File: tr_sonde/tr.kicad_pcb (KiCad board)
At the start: 4 copper layers, 104.4 x 65.3 mm, 87 parts, among them J1 SMA, J2 SMA, J3 SMA, K1 TR, K2 HV_MON, K3 VINHDR, Q1 PBSS4250X, Q2 MMBT2222A, Q3 STD2NK90ZT4, Q4 STD2NK90ZT4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

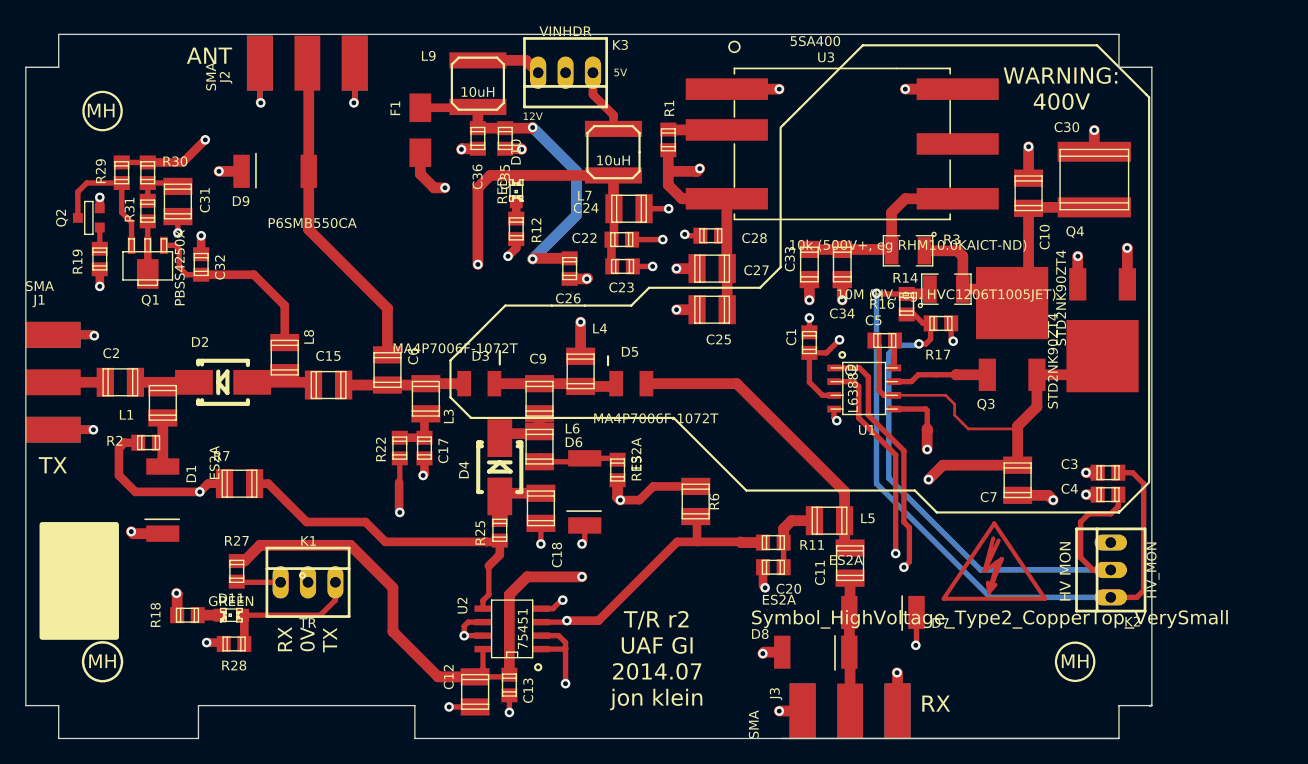
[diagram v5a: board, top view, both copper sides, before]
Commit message: added extra power header to control board, added spam to driver amp bottom soldermask layer to pass oshpark check script, added board outlines to agc and tr silkscreen
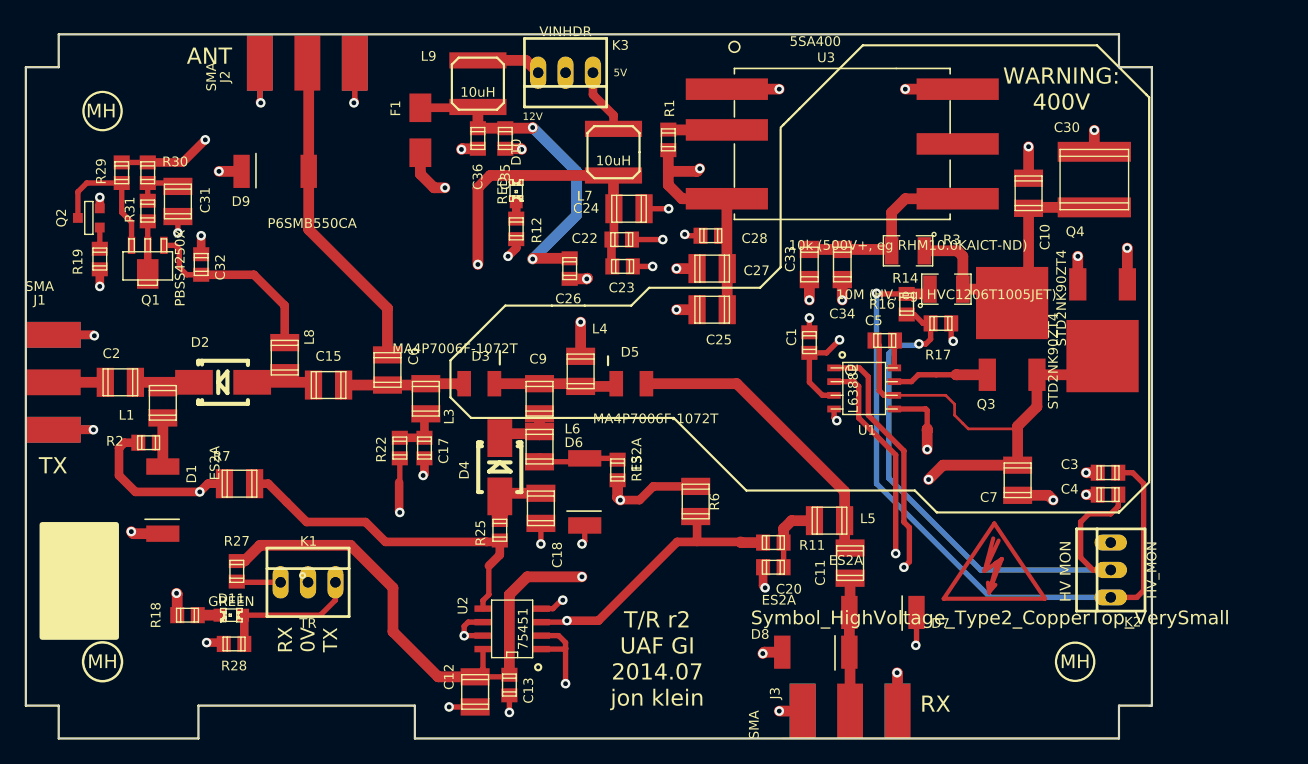
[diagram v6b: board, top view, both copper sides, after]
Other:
- rule trace_min: 0.18 -> 0.2

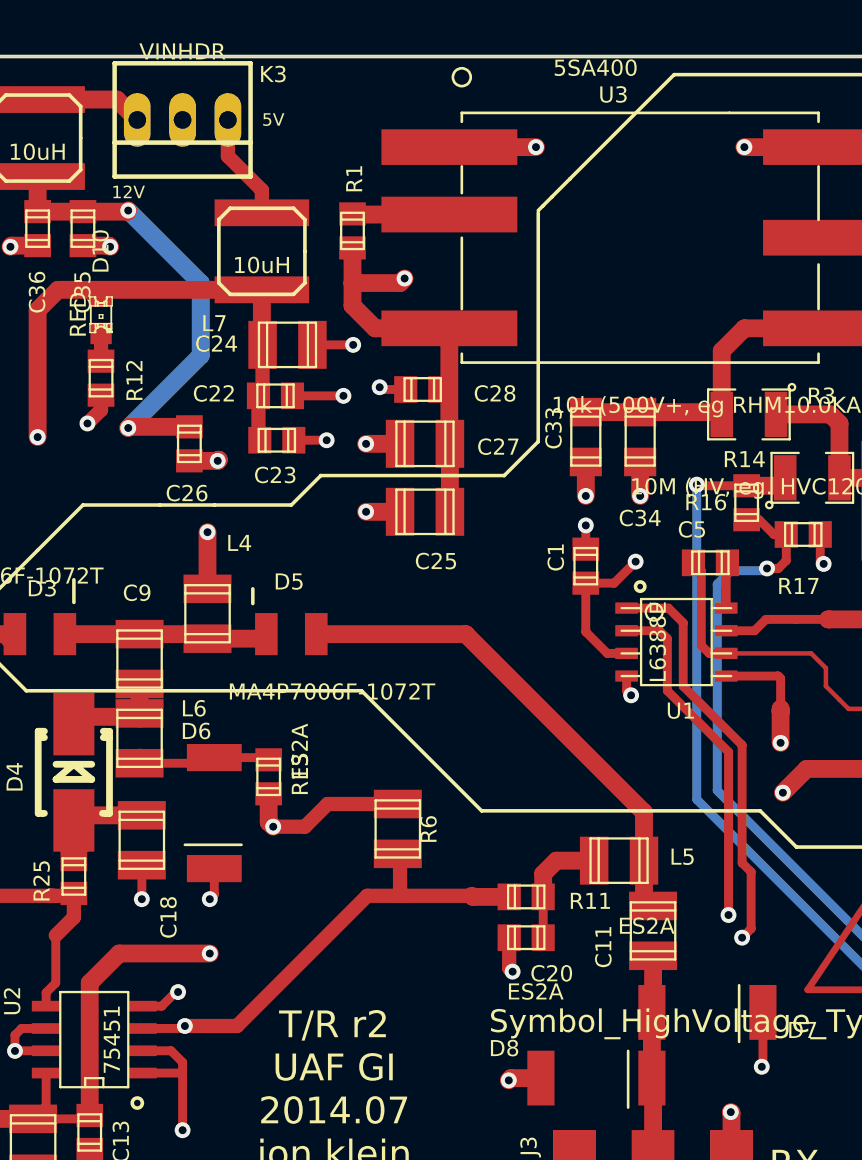
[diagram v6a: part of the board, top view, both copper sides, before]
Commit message: fixed footprints and silkscreen on t/r r2
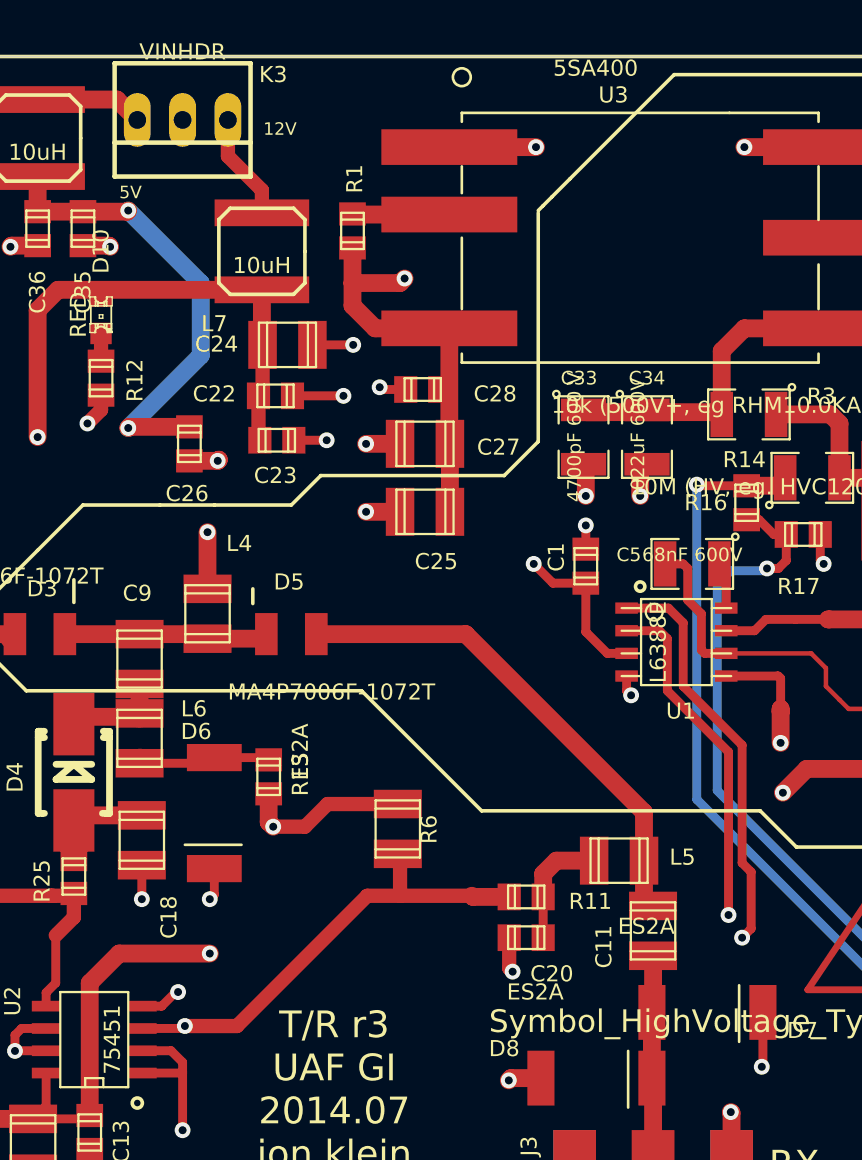
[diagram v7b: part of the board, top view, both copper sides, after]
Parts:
- C33: footprint Capacitors_SMD:c_1206 -> SMD_Packages:SMD-1210
- C34: footprint smd_capacitors:c_1206 -> SMD_Packages:SMD-1210
- C5: footprint smd_capacitors:c_0805 -> SMD_Packages:SMD-1210
- moved C5 1.02 mm to (135.8, 53.3), turned to 180 degrees
- moved C34 0.38 mm to (133.2, 46.2), turned to 270 degrees
- moved C33 0.13 mm to (129.7, 46.2), turned to 270 degrees
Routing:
- net VCC: track 205.8 -> 200.2 mm
- net /hvbias: track 92.7 -> 94.5 mm
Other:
- board text added: "T/R r3 UAF GI 2014.07 jon klein"
- board text added: "high power T/R switch r3"
- board text removed: "T/R r2 UAF GI 2014.07 jon klein"
- board text removed: "high power T/R switch r2"

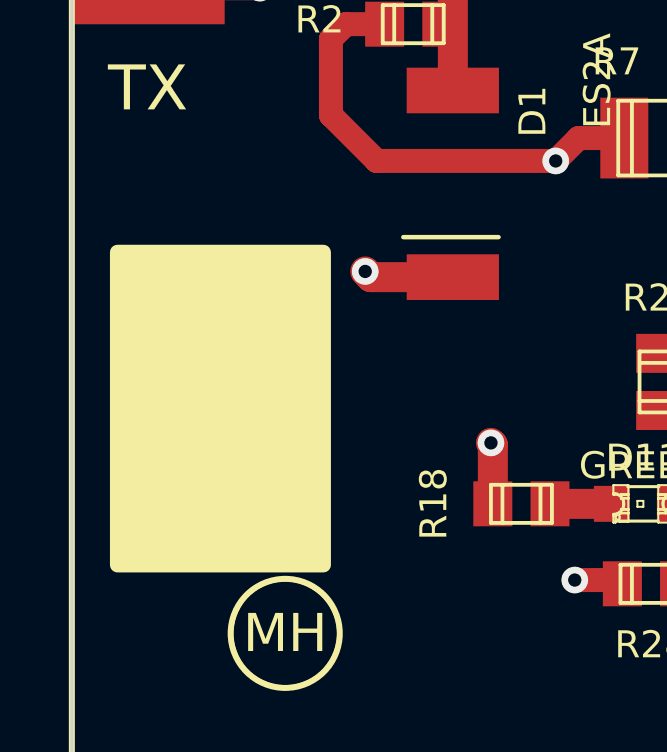
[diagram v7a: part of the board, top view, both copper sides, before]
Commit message: added power distribution board, changed SMA connectors to top through hole, moved mounting holes on rxfe
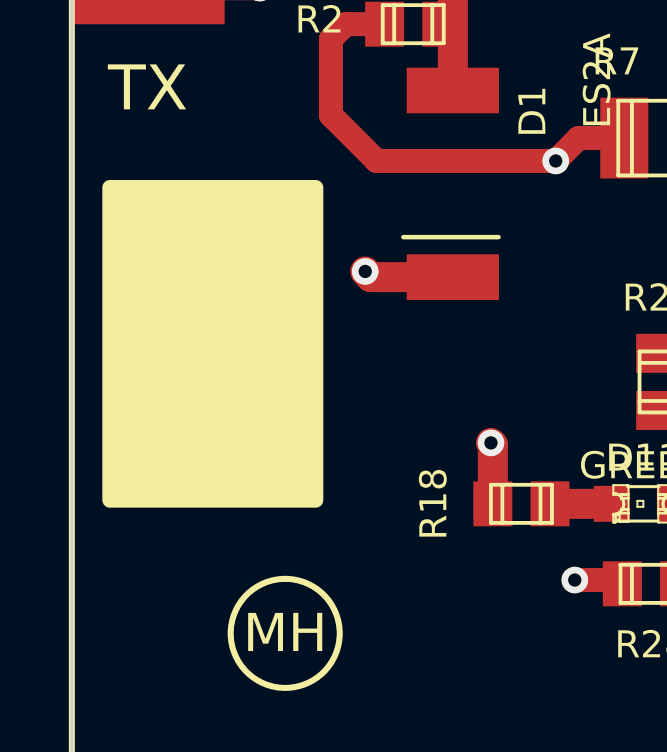
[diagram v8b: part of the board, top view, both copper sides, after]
